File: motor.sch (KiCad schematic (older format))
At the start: 44 parts, among them J5 70543-0003, Q10 PMPB11EN, Q11 PMPB11EN, Q4 PMPB11EN, Q5 PMPB11EN, Q6 PMPB11EN, Q7 PMPB11EN, Q8 PMPB11EN, Q9 PMPB11EN, U6 TMC2160-TA

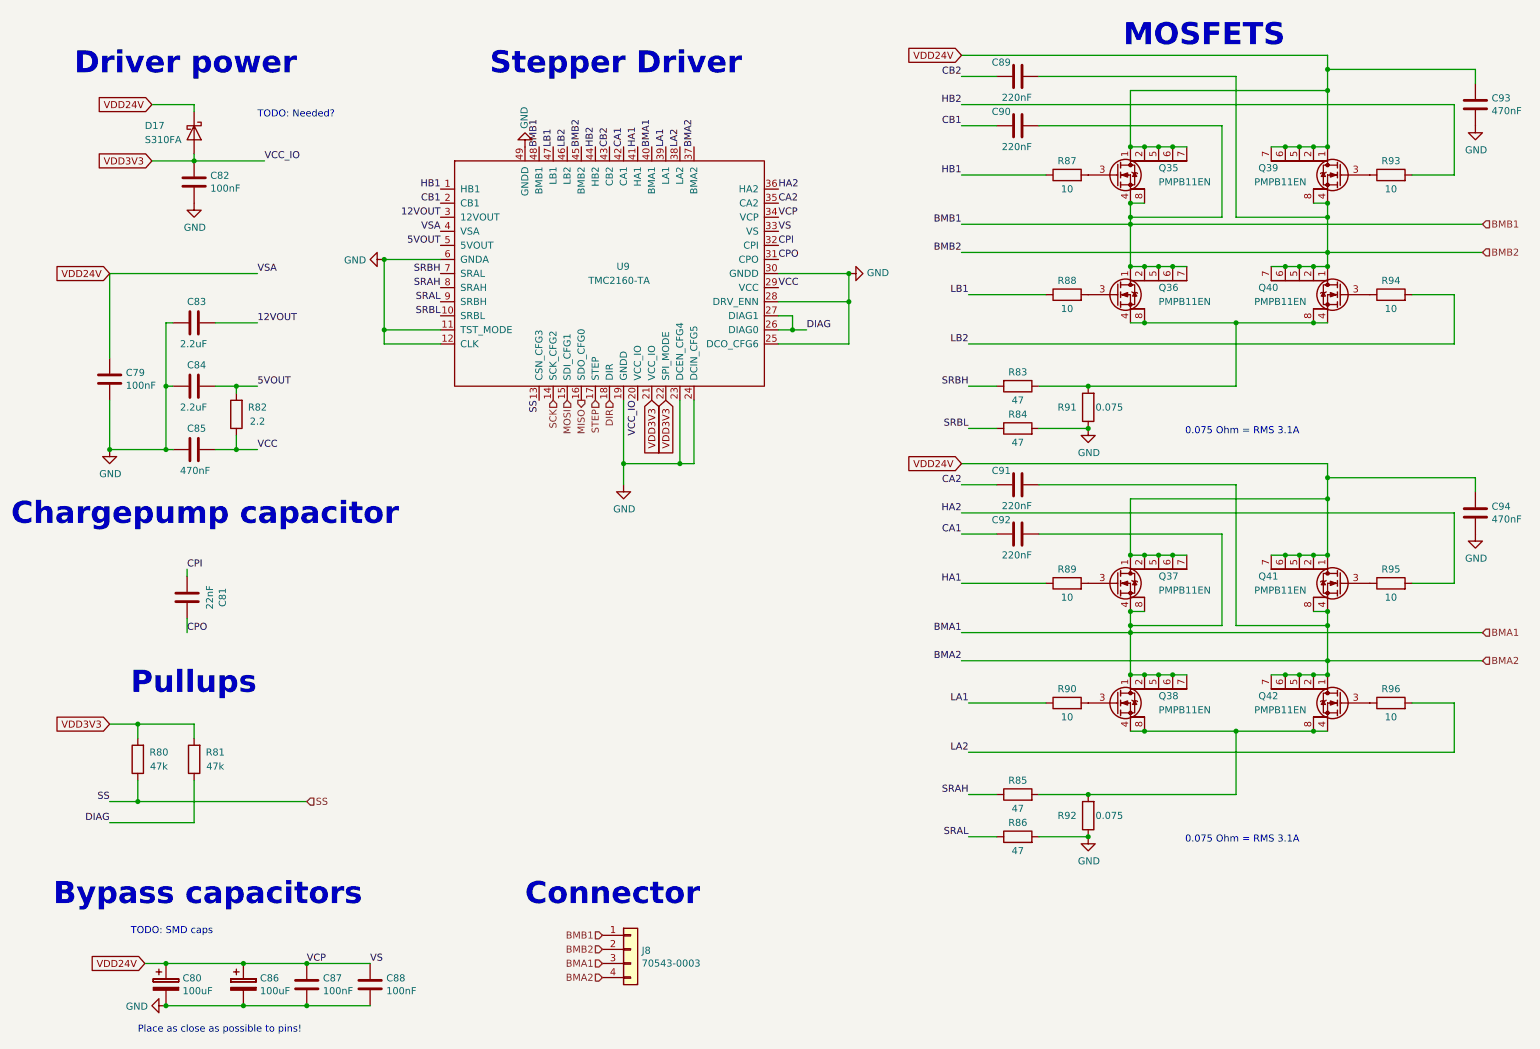
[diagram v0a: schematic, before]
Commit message: Fix various v1.0 errors
 * Change 3.3V LDO to AP7365-33WG-7
 * Optimize soldermask clearance (from 0.2 to 0.05)
 * Connect SD connect switch to GND
 * Optimized some PADs
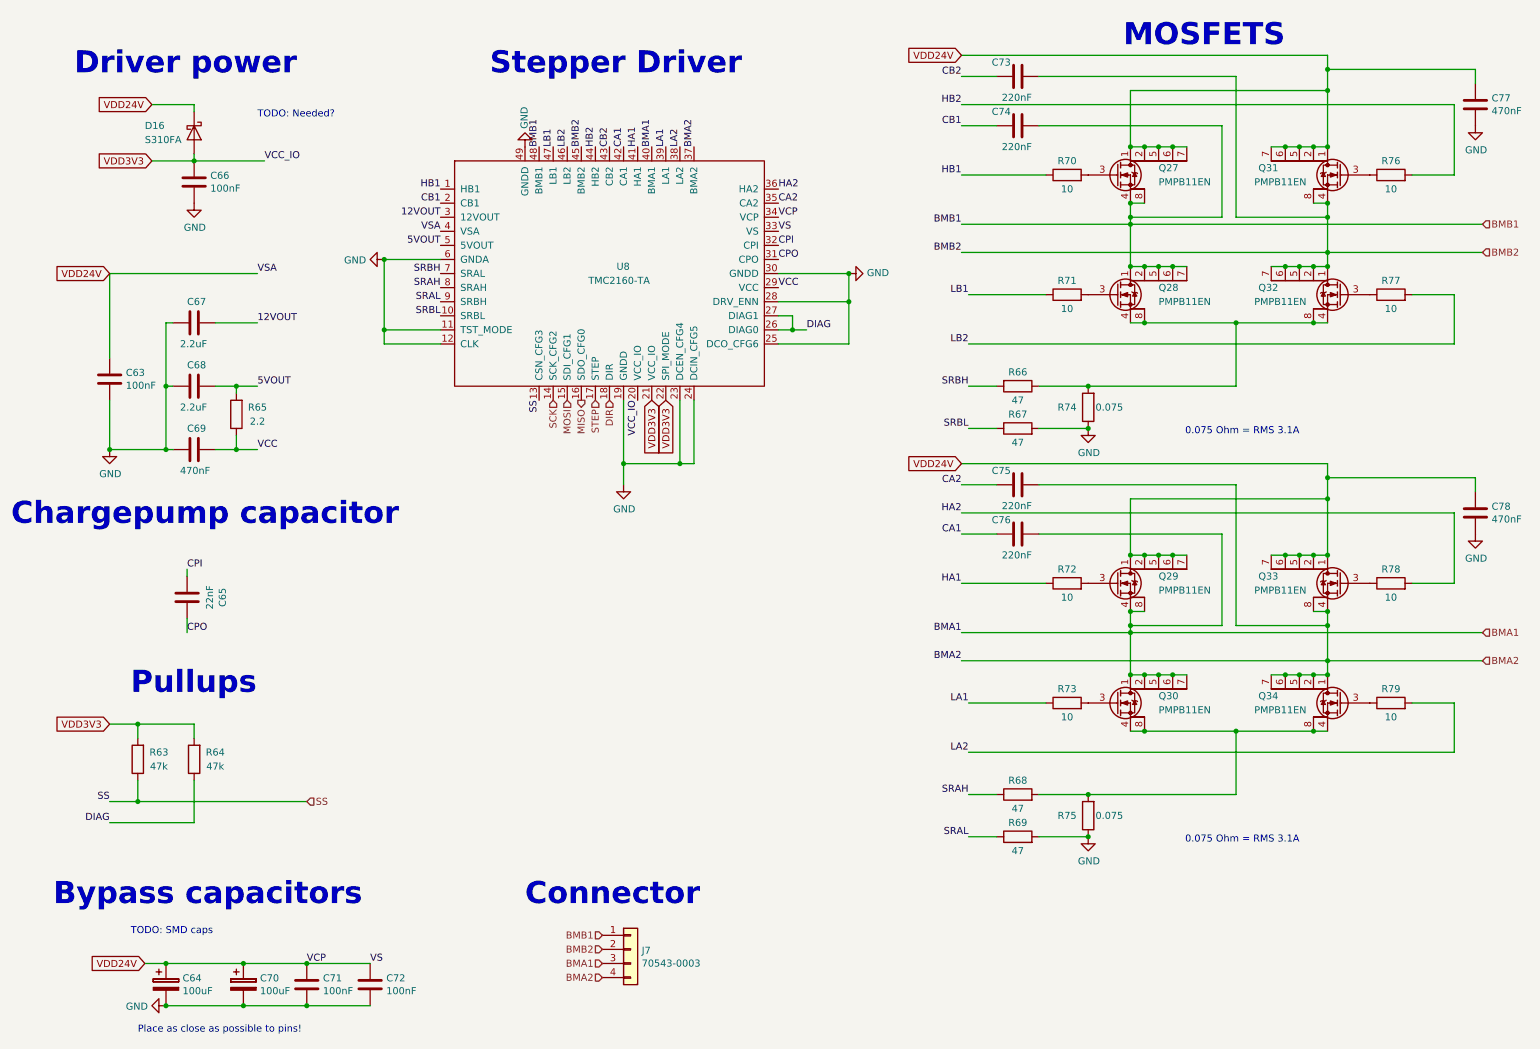
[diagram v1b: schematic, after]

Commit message: Updated board to version 1.2
 * Switched small MOSFETs to SOT-23 package
 * Redesigned TMC*160 driver layout
 * Changed 01x03 to 02x03 jumper for FAN voltage selection
 * Switches STATUS_LED pin
 * Some copper pour optimizations
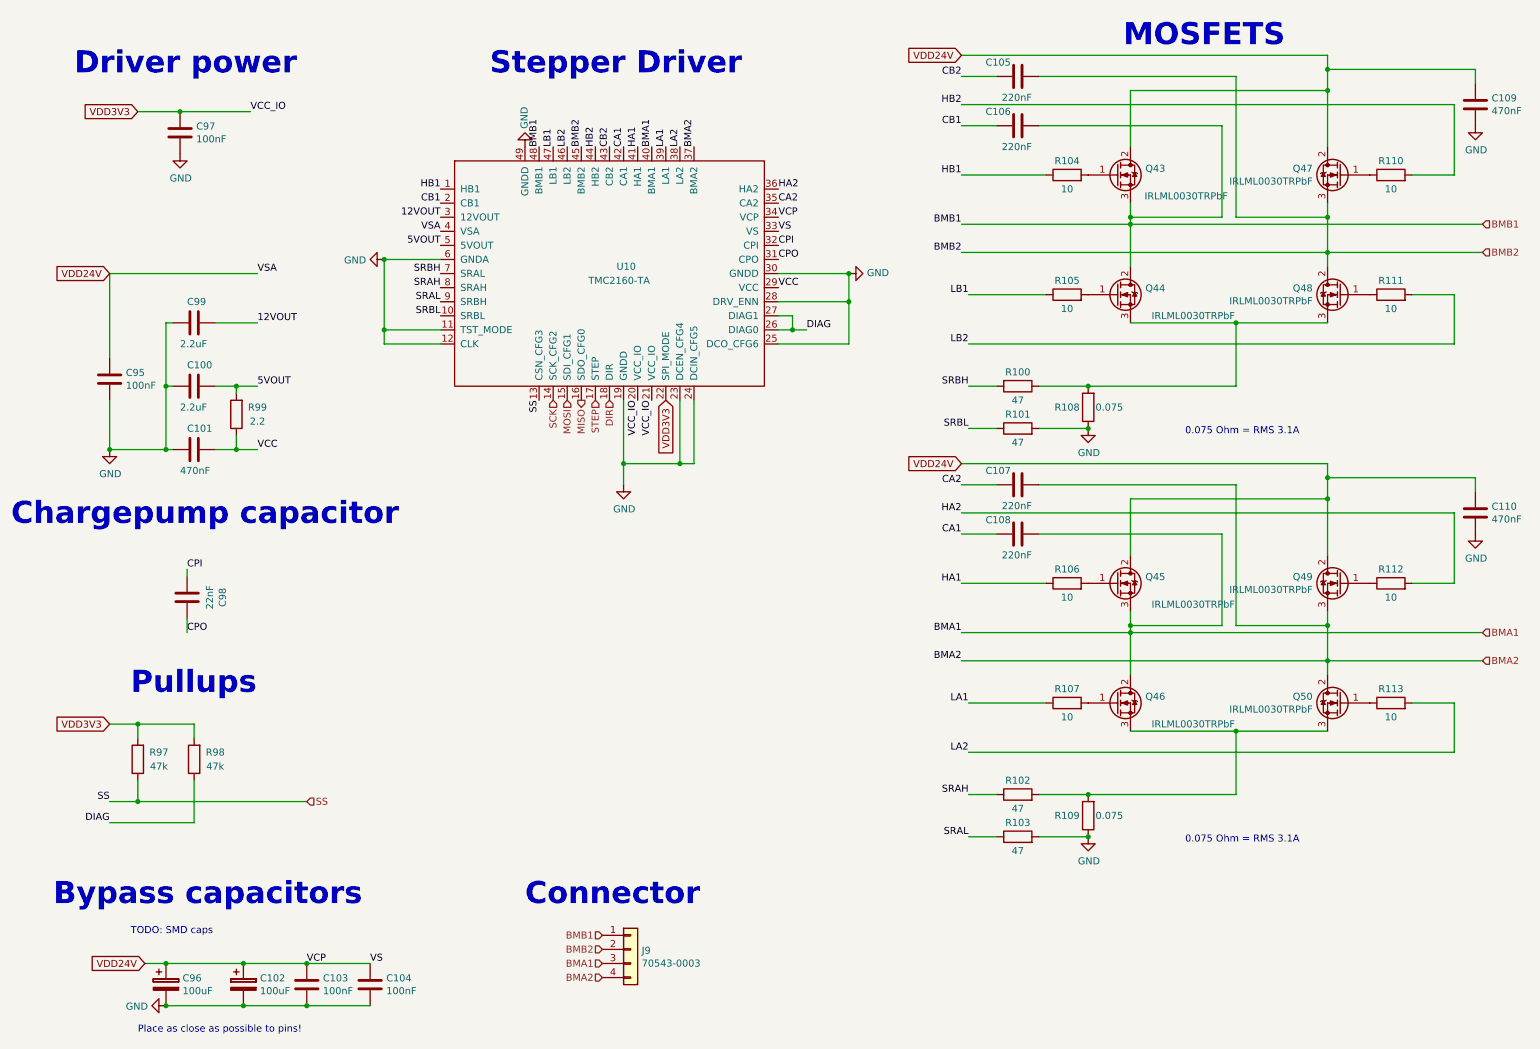
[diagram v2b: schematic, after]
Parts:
- removed D7: S310FA, Diode_SMD:D_SOD-123, symbol Device:D_Schottky
- removed Q10, Q11, Q4, Q5, Q6, Q7, Q8, Q9: PMPB11EN, heteromycin:SOT1220, symbol heteromycin:PMPB20EN
- added Q35, Q36, Q37, Q38, Q39, Q40, Q41, Q42: IRLML0030TRPbF, Package_TO_SOT_SMD:SOT-23, symbol Device:Q_NMOS_GDS
- C32, C38: footprint Capacitor_SMD:CP_Elec_6.3x5.7 -> Capacitor_THT:CP_Radial_D6.3mm_P2.50mm
- renumbered C34 to C33, C33 to C34
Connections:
- net BMA1: now also Q37.3 (S), Q38.2 (D)
- net BMA2: now also Q41.3 (S), Q42.2 (D)
- net BMB1: now also Q35.3 (S), Q36.2 (D)
- net BMB2: now also Q39.3 (S), Q40.2 (D)
- net VDD24V: now also Q35.2 (D), Q37.2 (D), Q39.2 (D), Q41.2 (D)
- net at R24.2: now also Q37.1 (G)
- net at R30.1: now also Q41.1 (G)
- net at R25.2: now also Q38.1 (G)
- net at R20.2, R27.2: now also Q38.3 (S), Q42.3 (S)
- net at R31.1: now also Q42.1 (G)
- net at R22.2: now also Q35.1 (G)
- net at R28.1: now also Q39.1 (G)
- net at R23.2: now also Q36.1 (G)
- net at R18.1, R26.2: now also Q36.3 (S), Q40.3 (S)
- net at R29.1: now also Q40.1 (G)
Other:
- note removed: "TODO: Needed?"
- moved on the sheet: C97

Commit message: Increased sense resistor value to 0.1
This will result in a maximum 2.3A current for the stepper.
This should act as a more sensible default. Of course the user
can replace the sense resistors as they see fit. As long as they
they don't stress the termal budget of the driver MOSFET that is.
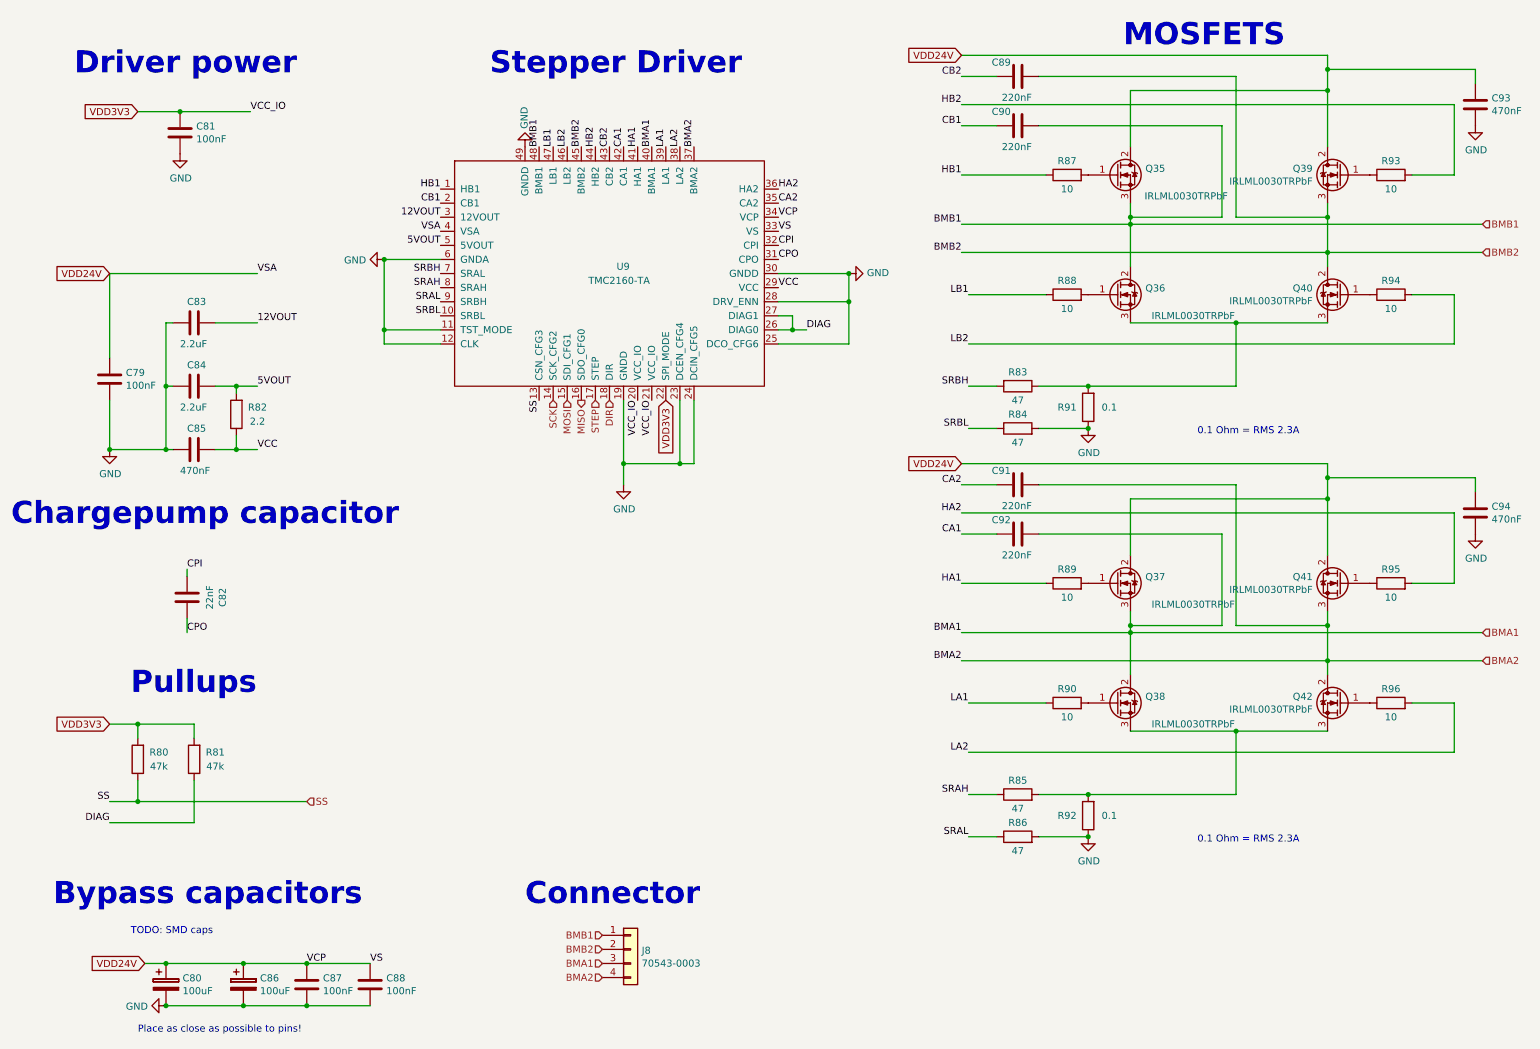
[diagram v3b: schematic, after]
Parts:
- R26, R27: value 0.075 -> 0.1
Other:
- note added: "0.1 Ohm = RMS 2.3A"
- note removed: "0.075 Ohm = RMS 3.1A"

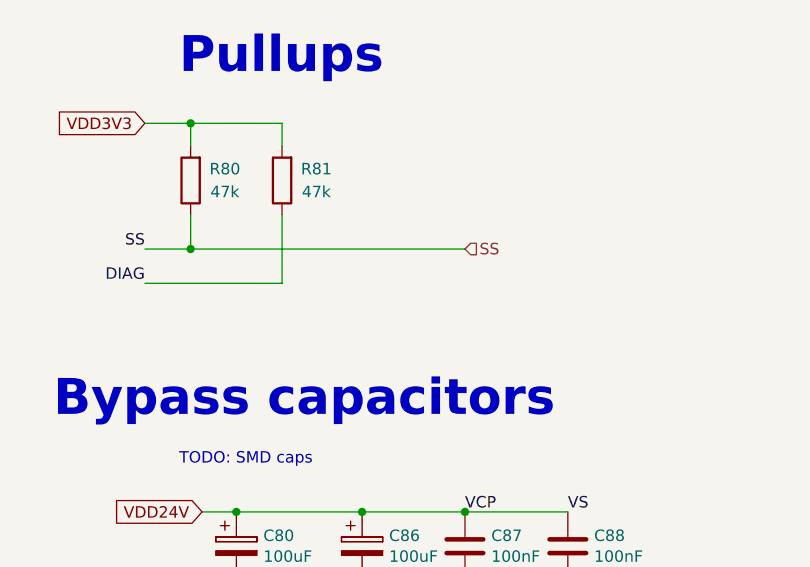
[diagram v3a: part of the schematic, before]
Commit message: Connected TMC DIAG pins to MCU
We had some pins free, so I decided to connect them, so that we
don't need to use the ENDSTOP OVER SPI feature.
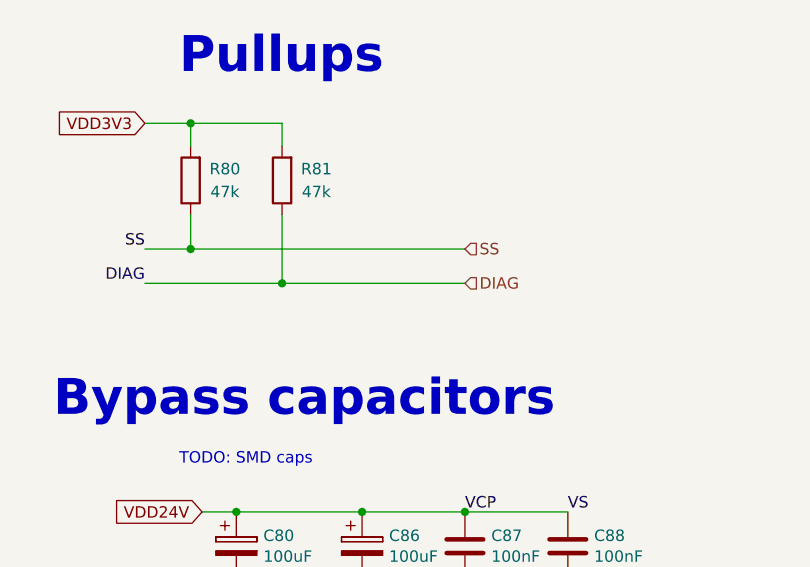
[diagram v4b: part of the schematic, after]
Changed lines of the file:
@@
 	1    0    0    -1
 $EndComp
+Text HLabel 2600 6200 2    50   Input ~ 0
+DIAG
+Wire Wire Line
+	2600 6200 1800 6200
+Connection ~ 1800 6200
 $EndSCHEMATC
